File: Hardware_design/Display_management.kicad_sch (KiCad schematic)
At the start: 0 parts

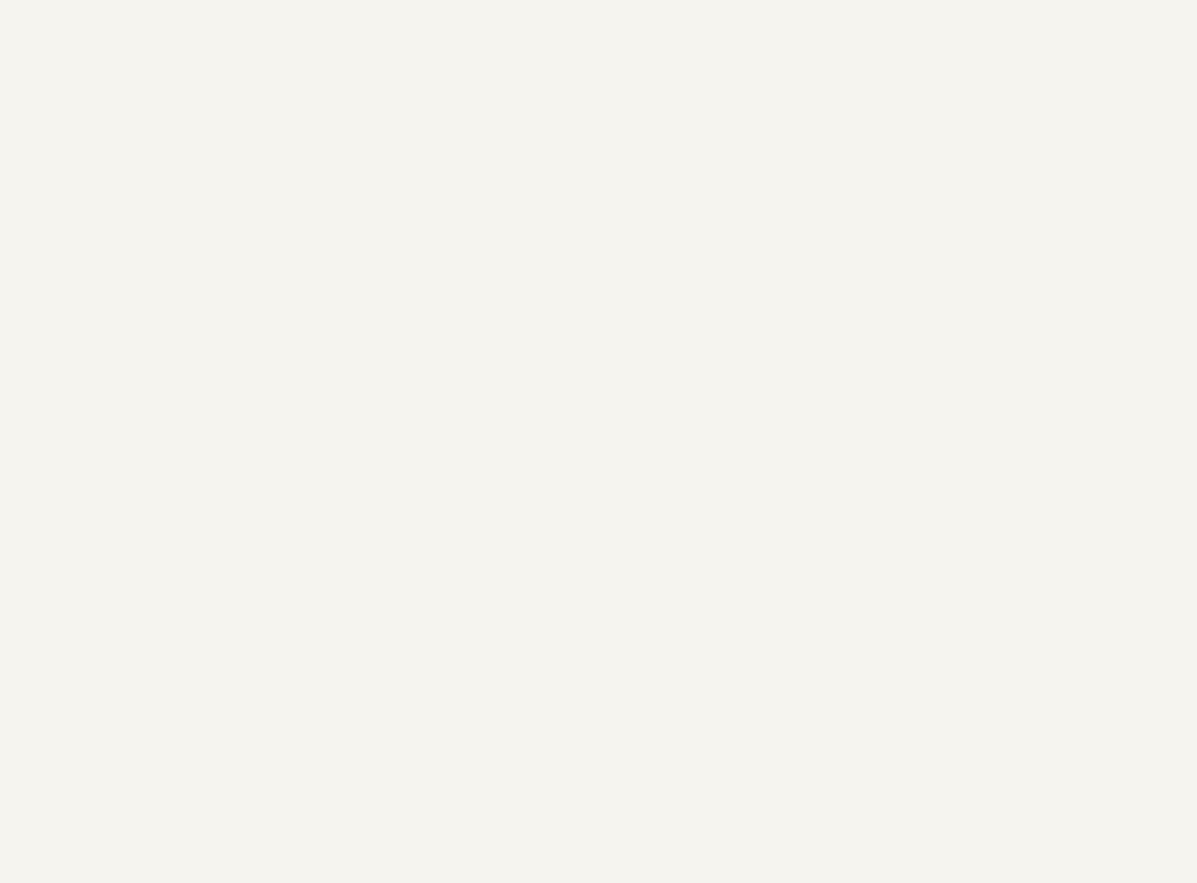
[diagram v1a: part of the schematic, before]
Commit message: STARTING THE DISPLAY design
acording to calculations we will need around 1.848 A when working with all the displays at the same time, including the MAX7221, the 1.848 A consumption is only for the display part.
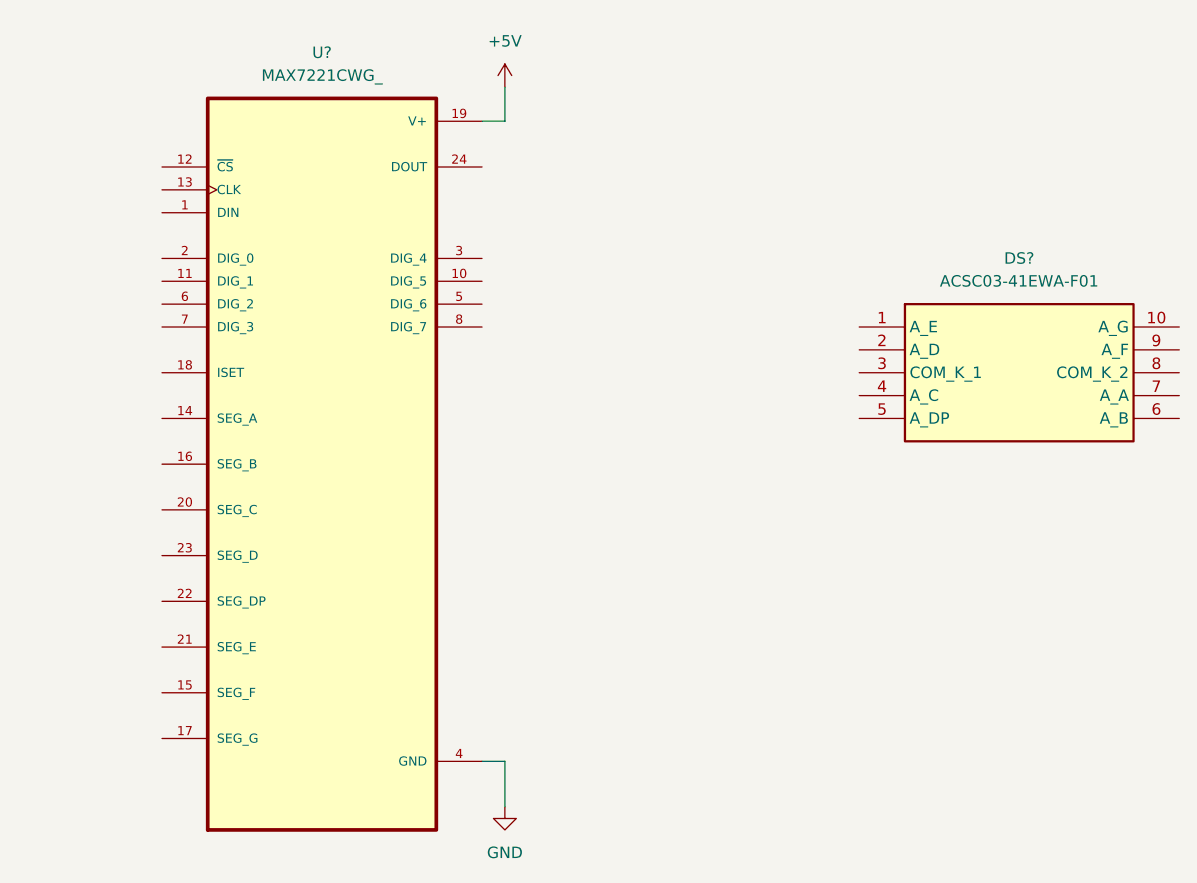
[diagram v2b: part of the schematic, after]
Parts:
- added DS?: ACSC03-41EWA-F01, ACSC0341EWAF01, symbol SMD_DISPLAY_ACSC03-41EWA-F01:ACSC03-41EWA-F01
- added U?: MAX7221CWG_, MAX7221CWG_:SOIC127P1032X265-24N, symbol Disp_Controler_MAX7221CWG_:MAX7221CWG_
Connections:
- new net +5V: U?.19 (V+)
- new net GND: U?.4 (GND), U?.9 (GND)

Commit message: display set up completed
for the displays we will not need an aditional voltage regulator becuase we will use the direct conection from the 5V power supply of the circuit, it needs to be able to provide at least 3A, recomended will be 4A for all the displays and pcb chips to work properly
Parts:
- added C? (x11): 0.1 uF, symbol Device:C
- added DS? (x84): ACSC03-41EWA-F01, ACSC0341EWAF01, symbol SMD_DISPLAY_ACSC03-41EWA-F01:ACSC03-41EWA-F01
- added R? (x11): 3v=24.5k, 1.8v=29.8k, symbol Device:R
- added U? (x10): MAX7221CWG_, MAX7221CWG_:SOIC127P1032X265-24N, symbol Disp_Controler_MAX7221CWG_:MAX7221CWG_
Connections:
- net +5V: now also C?.1, C?.1, C?.1, C?.1, C?.1, C?.1, C?.1, C?.1, C?.1, C?.1, C?.1, R?.1, R?.1, R?.1, R?.1, R?.1, R?.1, R?.1, R?.1, R?.1, R?.1, R?.1, U?.19 (V+), U?.19 (V+), U?.19 (V+), U?.19 (V+), U?.19 (V+), U?.19 (V+), U?.19 (V+), U?.19 (V+), U?.19 (V+), U?.19 (V+)
- net CS_MAX7221: now also U?.12 (~{CS}), U?.12 (~{CS}), U?.12 (~{CS}), U?.12 (~{CS}), U?.12 (~{CS}), U?.12 (~{CS}), U?.12 (~{CS}), U?.12 (~{CS}), U?.12 (~{CS}), U?.12 (~{CS}), U?.12 (~{CS})
- net GND: now also C?.2, C?.2, C?.2, C?.2, C?.2, C?.2, C?.2, C?.2, C?.2, C?.2, C?.2, U?.4 (GND), U?.4 (GND), U?.4 (GND), U?.4 (GND), U?.4 (GND), U?.4 (GND), U?.4 (GND), U?.4 (GND), U?.4 (GND), U?.4 (GND), U?.9 (GND), U?.9 (GND), U?.9 (GND), U?.9 (GND), U?.9 (GND), U?.9 (GND), U?.9 (GND), U?.9 (GND), U?.9 (GND), U?.9 (GND)
- net MOSI_MAX7221: now also U?.1 (DIN)
- net SCK_MAX7221: now also U?.13 (CLK), U?.13 (CLK), U?.13 (CLK), U?.13 (CLK), U?.13 (CLK), U?.13 (CLK), U?.13 (CLK), U?.13 (CLK), U?.13 (CLK), U?.13 (CLK), U?.13 (CLK)
- net DIG_5_MAX7221_1: now reaches U?.10 (DIG_5)
- net DIG_5_MAX7221_1: now also DS?.3 (COM_K_1), DS?.8 (COM_K_2)
- net DIG_1_MAX7221_1: now reaches U?.11 (DIG_1)
- net DIG_1_MAX7221_1: now also DS?.3 (COM_K_1), DS?.8 (COM_K_2)
- net SEG_A_MAX7221_1: now reaches U?.14 (SEG_A)
- net SEG_A_MAX7221_1: now also DS?.7 (A_A), DS?.7 (A_A), DS?.7 (A_A), DS?.7 (A_A), DS?.7 (A_A), DS?.7 (A_A), DS?.7 (A_A), DS?.7 (A_A)
- net SEG_F_MAX7221_1: now reaches U?.15 (SEG_F)
- net SEG_F_MAX7221_1: now also DS?.9 (A_F), DS?.9 (A_F), DS?.9 (A_F), DS?.9 (A_F), DS?.9 (A_F), DS?.9 (A_F), DS?.9 (A_F), DS?.9 (A_F)
- net SEG_B_MAX7221_1: now reaches U?.16 (SEG_B)
- net SEG_B_MAX7221_1: now also DS?.6 (A_B), DS?.6 (A_B), DS?.6 (A_B), DS?.6 (A_B), DS?.6 (A_B), DS?.6 (A_B), DS?.6 (A_B), DS?.6 (A_B)
- net SEG_G_MAX7221_1: now reaches U?.17 (SEG_G)
- net SEG_G_MAX7221_1: now also DS?.10 (A_G), DS?.10 (A_G), DS?.10 (A_G), DS?.10 (A_G), DS?.10 (A_G), DS?.10 (A_G), DS?.10 (A_G), DS?.10 (A_G)
- net at U?.18 (ISET): now also R?.2
- net DIG_0_MAX7221_1: now reaches U?.2 (DIG_0)
- net DIG_0_MAX7221_1: now also DS?.3 (COM_K_1), DS?.8 (COM_K_2)
- net SEG_C_MAX7221_1: now reaches U?.20 (SEG_C)
- net SEG_C_MAX7221_1: now also DS?.4 (A_C), DS?.4 (A_C), DS?.4 (A_C), DS?.4 (A_C), DS?.4 (A_C), DS?.4 (A_C), DS?.4 (A_C), DS?.4 (A_C)
- net SEG_E_MAX7221_1: now reaches U?.21 (SEG_E)
- net SEG_E_MAX7221_1: now also DS?.1 (A_E), DS?.1 (A_E), DS?.1 (A_E), DS?.1 (A_E), DS?.1 (A_E), DS?.1 (A_E), DS?.1 (A_E), DS?.1 (A_E)
- net SEG_DP_MAX7221_1: now reaches U?.22 (SEG_DP)
- net SEG_DP_MAX7221_1: now also DS?.5 (A_DP), DS?.5 (A_DP), DS?.5 (A_DP), DS?.5 (A_DP), DS?.5 (A_DP), DS?.5 (A_DP), DS?.5 (A_DP), DS?.5 (A_DP)
- net SEG_D_MAX7221_1: now reaches U?.23 (SEG_D)
- net SEG_D_MAX7221_1: now also DS?.2 (A_D), DS?.2 (A_D), DS?.2 (A_D), DS?.2 (A_D), DS?.2 (A_D), DS?.2 (A_D), DS?.2 (A_D), DS?.2 (A_D)
- net at U?.24 (DOUT): now also U?.1 (DIN)
- net DIG_4_MAX7221_1: now reaches U?.3 (DIG_4)
- net DIG_4_MAX7221_1: now also DS?.3 (COM_K_1), DS?.8 (COM_K_2)
- net DIG_6_MAX7221_1: now reaches U?.5 (DIG_6)
- net DIG_6_MAX7221_1: now also DS?.3 (COM_K_1), DS?.8 (COM_K_2)
- net DIG_2_MAX7221_1: now reaches U?.6 (DIG_2)
- net DIG_2_MAX7221_1: now also DS?.3 (COM_K_1), DS?.8 (COM_K_2)
- net DIG_3_MAX7221_1: now reaches U?.7 (DIG_3)
- net DIG_3_MAX7221_1: now also DS?.3 (COM_K_1), DS?.8 (COM_K_2)
- net DIG_7_MAX7221_1: now reaches U?.8 (DIG_7)
- net DIG_7_MAX7221_1: now also DS?.3 (COM_K_1), DS?.8 (COM_K_2)
- new net: R?.2, U?.18 (ISET) (x10)
- new net: U?.1 (DIN), U?.24 (DOUT) (x9)
- new net DIG_0_MAX7221_10: DS?.3 (COM_K_1), DS?.8 (COM_K_2), U?.2 (DIG_0)
- new net DIG_0_MAX7221_11: DS?.3 (COM_K_1), DS?.8 (COM_K_2), U?.2 (DIG_0)
- new net DIG_0_MAX7221_2: DS?.3 (COM_K_1), DS?.8 (COM_K_2), U?.2 (DIG_0)
- new net DIG_0_MAX7221_3: DS?.3 (COM_K_1), DS?.8 (COM_K_2), U?.2 (DIG_0)
- new net DIG_0_MAX7221_4: DS?.3 (COM_K_1), DS?.8 (COM_K_2), U?.2 (DIG_0)
- new net DIG_0_MAX7221_5: DS?.3 (COM_K_1), DS?.8 (COM_K_2), U?.2 (DIG_0)
- new net DIG_0_MAX7221_6: DS?.3 (COM_K_1), DS?.8 (COM_K_2), U?.2 (DIG_0)
- new net DIG_0_MAX7221_7: DS?.3 (COM_K_1), DS?.8 (COM_K_2), U?.2 (DIG_0)
- new net DIG_0_MAX7221_8: DS?.3 (COM_K_1), DS?.8 (COM_K_2), U?.2 (DIG_0)
- new net DIG_0_MAX7221_9: DS?.3 (COM_K_1), DS?.8 (COM_K_2), U?.2 (DIG_0)
- new net DIG_1_MAX7221_10: DS?.3 (COM_K_1), DS?.8 (COM_K_2), U?.11 (DIG_1)
- new net DIG_1_MAX7221_11: DS?.3 (COM_K_1), DS?.8 (COM_K_2), U?.11 (DIG_1)
- new net DIG_1_MAX7221_2: DS?.3 (COM_K_1), DS?.8 (COM_K_2), U?.11 (DIG_1)
- new net DIG_1_MAX7221_3: DS?.3 (COM_K_1), DS?.8 (COM_K_2), U?.11 (DIG_1)
- new net DIG_1_MAX7221_4: DS?.3 (COM_K_1), DS?.8 (COM_K_2), U?.11 (DIG_1)
- new net DIG_1_MAX7221_5: DS?.3 (COM_K_1), DS?.8 (COM_K_2), U?.11 (DIG_1)
- new net DIG_1_MAX7221_6: DS?.3 (COM_K_1), DS?.8 (COM_K_2), U?.11 (DIG_1)
- new net DIG_1_MAX7221_7: DS?.3 (COM_K_1), DS?.8 (COM_K_2), U?.11 (DIG_1)
- new net DIG_1_MAX7221_8: DS?.3 (COM_K_1), DS?.8 (COM_K_2), U?.11 (DIG_1)
- new net DIG_1_MAX7221_9: DS?.3 (COM_K_1), DS?.8 (COM_K_2), U?.11 (DIG_1)
- new net DIG_2_MAX7221_10: DS?.3 (COM_K_1), DS?.8 (COM_K_2), U?.6 (DIG_2)
- new net DIG_2_MAX7221_11: DS?.3 (COM_K_1), DS?.8 (COM_K_2), U?.6 (DIG_2)
- new net DIG_2_MAX7221_2: DS?.3 (COM_K_1), DS?.8 (COM_K_2), U?.6 (DIG_2)
- new net DIG_2_MAX7221_3: DS?.3 (COM_K_1), DS?.8 (COM_K_2), U?.6 (DIG_2)
- new net DIG_2_MAX7221_4: DS?.3 (COM_K_1), DS?.8 (COM_K_2), U?.6 (DIG_2)
- new net DIG_2_MAX7221_5: DS?.3 (COM_K_1), DS?.8 (COM_K_2), U?.6 (DIG_2)
- new net DIG_2_MAX7221_6: DS?.3 (COM_K_1), DS?.8 (COM_K_2), U?.6 (DIG_2)
- new net DIG_2_MAX7221_7: DS?.3 (COM_K_1), DS?.8 (COM_K_2), U?.6 (DIG_2)
- new net DIG_2_MAX7221_8: DS?.3 (COM_K_1), DS?.8 (COM_K_2), U?.6 (DIG_2)
- new net DIG_2_MAX7221_9: DS?.3 (COM_K_1), DS?.8 (COM_K_2), U?.6 (DIG_2)
- new net DIG_3_MAX7221_10: DS?.3 (COM_K_1), DS?.8 (COM_K_2), U?.7 (DIG_3)
- new net DIG_3_MAX7221_11: DS?.3 (COM_K_1), DS?.8 (COM_K_2), U?.7 (DIG_3)
- new net DIG_3_MAX7221_2: DS?.3 (COM_K_1), DS?.8 (COM_K_2), U?.7 (DIG_3)
- new net DIG_3_MAX7221_3: DS?.3 (COM_K_1), DS?.8 (COM_K_2), U?.7 (DIG_3)
- new net DIG_3_MAX7221_4: DS?.3 (COM_K_1), DS?.8 (COM_K_2), U?.7 (DIG_3)
- new net DIG_3_MAX7221_5: DS?.3 (COM_K_1), DS?.8 (COM_K_2), U?.7 (DIG_3)
- new net DIG_3_MAX7221_6: DS?.3 (COM_K_1), DS?.8 (COM_K_2), U?.7 (DIG_3)
- new net DIG_3_MAX7221_7: DS?.3 (COM_K_1), DS?.8 (COM_K_2), U?.7 (DIG_3)
- new net DIG_3_MAX7221_8: DS?.3 (COM_K_1), DS?.8 (COM_K_2), U?.7 (DIG_3)
- new net DIG_3_MAX7221_9: DS?.3 (COM_K_1), DS?.8 (COM_K_2), U?.7 (DIG_3)
- new net DIG_4_MAX7221_10: DS?.3 (COM_K_1), DS?.8 (COM_K_2), U?.3 (DIG_4)
- new net DIG_4_MAX7221_11: DS?.3 (COM_K_1), DS?.8 (COM_K_2), U?.3 (DIG_4)
- new net DIG_4_MAX7221_2: DS?.3 (COM_K_1), DS?.8 (COM_K_2), U?.3 (DIG_4)
- new net DIG_4_MAX7221_3: DS?.3 (COM_K_1), DS?.8 (COM_K_2), U?.3 (DIG_4)
- new net DIG_4_MAX7221_4: DS?.3 (COM_K_1), DS?.8 (COM_K_2), U?.3 (DIG_4)
- new net DIG_4_MAX7221_5: DS?.3 (COM_K_1), DS?.8 (COM_K_2), U?.3 (DIG_4)
- new net DIG_4_MAX7221_6: DS?.3 (COM_K_1), DS?.8 (COM_K_2), U?.3 (DIG_4)
- new net DIG_4_MAX7221_7: DS?.3 (COM_K_1), DS?.8 (COM_K_2), U?.3 (DIG_4)
- new net DIG_4_MAX7221_8: DS?.3 (COM_K_1), DS?.8 (COM_K_2), U?.3 (DIG_4)
- new net DIG_4_MAX7221_9: DS?.3 (COM_K_1), DS?.8 (COM_K_2), U?.3 (DIG_4)
- new net DIG_5_MAX7221_10: DS?.3 (COM_K_1), DS?.8 (COM_K_2), U?.10 (DIG_5)
- new net DIG_5_MAX7221_11: U?.10 (DIG_5)
- new net DIG_5_MAX7221_2: DS?.3 (COM_K_1), DS?.8 (COM_K_2), U?.10 (DIG_5)
- new net DIG_5_MAX7221_3: DS?.3 (COM_K_1), DS?.8 (COM_K_2), U?.10 (DIG_5)
- new net DIG_5_MAX7221_4: DS?.3 (COM_K_1), DS?.8 (COM_K_2), U?.10 (DIG_5)
- new net DIG_5_MAX7221_5: DS?.3 (COM_K_1), DS?.8 (COM_K_2), U?.10 (DIG_5)
- new net DIG_5_MAX7221_6: DS?.3 (COM_K_1), DS?.8 (COM_K_2), U?.10 (DIG_5)
- new net DIG_5_MAX7221_7: DS?.3 (COM_K_1), DS?.8 (COM_K_2), U?.10 (DIG_5)
- new net DIG_5_MAX7221_8: DS?.3 (COM_K_1), DS?.8 (COM_K_2), U?.10 (DIG_5)
- new net DIG_5_MAX7221_9: DS?.3 (COM_K_1), DS?.8 (COM_K_2), U?.10 (DIG_5)
- new net DIG_6_MAX7221_10: DS?.3 (COM_K_1), DS?.8 (COM_K_2), U?.5 (DIG_6)
- new net DIG_6_MAX7221_11: U?.5 (DIG_6)
- new net DIG_6_MAX7221_2: DS?.3 (COM_K_1), DS?.8 (COM_K_2), U?.5 (DIG_6)
- new net DIG_6_MAX7221_3: DS?.3 (COM_K_1), DS?.8 (COM_K_2), U?.5 (DIG_6)
- new net DIG_6_MAX7221_4: DS?.3 (COM_K_1), DS?.8 (COM_K_2), U?.5 (DIG_6)
- new net DIG_6_MAX7221_5: DS?.3 (COM_K_1), DS?.8 (COM_K_2), U?.5 (DIG_6)
- new net DIG_6_MAX7221_6: DS?.3 (COM_K_1), DS?.8 (COM_K_2), U?.5 (DIG_6)
- new net DIG_6_MAX7221_7: DS?.3 (COM_K_1), DS?.8 (COM_K_2), U?.5 (DIG_6)
- new net DIG_6_MAX7221_8: DS?.3 (COM_K_1), DS?.8 (COM_K_2), U?.5 (DIG_6)
- new net DIG_6_MAX7221_9: DS?.3 (COM_K_1), DS?.8 (COM_K_2), U?.5 (DIG_6)
- new net DIG_7_MAX7221_10: DS?.3 (COM_K_1), DS?.8 (COM_K_2), U?.8 (DIG_7)
- new net DIG_7_MAX7221_11: U?.8 (DIG_7)
- new net DIG_7_MAX7221_2: DS?.3 (COM_K_1), DS?.8 (COM_K_2), U?.8 (DIG_7)
- new net DIG_7_MAX7221_3: DS?.3 (COM_K_1), DS?.8 (COM_K_2), U?.8 (DIG_7)
- new net DIG_7_MAX7221_4: DS?.3 (COM_K_1), DS?.8 (COM_K_2), U?.8 (DIG_7)
- new net DIG_7_MAX7221_5: DS?.3 (COM_K_1), DS?.8 (COM_K_2), U?.8 (DIG_7)
- new net DIG_7_MAX7221_6: DS?.3 (COM_K_1), DS?.8 (COM_K_2), U?.8 (DIG_7)
- new net DIG_7_MAX7221_7: DS?.3 (COM_K_1), DS?.8 (COM_K_2), U?.8 (DIG_7)
- new net DIG_7_MAX7221_8: DS?.3 (COM_K_1), DS?.8 (COM_K_2), U?.8 (DIG_7)
- new net DIG_7_MAX7221_9: DS?.3 (COM_K_1), DS?.8 (COM_K_2), U?.8 (DIG_7)
- new net SEG_A_MAX7221_10: DS?.7 (A_A), DS?.7 (A_A), DS?.7 (A_A), DS?.7 (A_A), DS?.7 (A_A), DS?.7 (A_A), DS?.7 (A_A), DS?.7 (A_A), U?.14 (SEG_A)
- new net SEG_A_MAX7221_11: DS?.7 (A_A), DS?.7 (A_A), DS?.7 (A_A), DS?.7 (A_A), DS?.7 (A_A), U?.14 (SEG_A)
- new net SEG_A_MAX7221_2: DS?.7 (A_A), DS?.7 (A_A), DS?.7 (A_A), DS?.7 (A_A), DS?.7 (A_A), DS?.7 (A_A), DS?.7 (A_A), DS?.7 (A_A), U?.14 (SEG_A)
- new net SEG_A_MAX7221_3: DS?.7 (A_A), DS?.7 (A_A), DS?.7 (A_A), DS?.7 (A_A), DS?.7 (A_A), DS?.7 (A_A), DS?.7 (A_A), DS?.7 (A_A), U?.14 (SEG_A)
- new net SEG_A_MAX7221_4: DS?.7 (A_A), DS?.7 (A_A), DS?.7 (A_A), DS?.7 (A_A), DS?.7 (A_A), DS?.7 (A_A), DS?.7 (A_A), DS?.7 (A_A), U?.14 (SEG_A)
- new net SEG_A_MAX7221_5: DS?.7 (A_A), DS?.7 (A_A), DS?.7 (A_A), DS?.7 (A_A), DS?.7 (A_A), DS?.7 (A_A), DS?.7 (A_A), DS?.7 (A_A), U?.14 (SEG_A)
- new net SEG_A_MAX7221_6: DS?.7 (A_A), DS?.7 (A_A), DS?.7 (A_A), DS?.7 (A_A), DS?.7 (A_A), DS?.7 (A_A), DS?.7 (A_A), DS?.7 (A_A), U?.14 (SEG_A)
- new net SEG_A_MAX7221_7: DS?.7 (A_A), DS?.7 (A_A), DS?.7 (A_A), DS?.7 (A_A), DS?.7 (A_A), DS?.7 (A_A), DS?.7 (A_A), DS?.7 (A_A), U?.14 (SEG_A)
- new net SEG_A_MAX7221_8: DS?.7 (A_A), DS?.7 (A_A), DS?.7 (A_A), DS?.7 (A_A), DS?.7 (A_A), DS?.7 (A_A), DS?.7 (A_A), DS?.7 (A_A), U?.14 (SEG_A)
- new net SEG_A_MAX7221_9: DS?.7 (A_A), DS?.7 (A_A), DS?.7 (A_A), DS?.7 (A_A), DS?.7 (A_A), DS?.7 (A_A), DS?.7 (A_A), DS?.7 (A_A), U?.14 (SEG_A)
- new net SEG_B_MAX7221_10: DS?.6 (A_B), DS?.6 (A_B), DS?.6 (A_B), DS?.6 (A_B), DS?.6 (A_B), DS?.6 (A_B), DS?.6 (A_B), DS?.6 (A_B), U?.16 (SEG_B)
- new net SEG_B_MAX7221_11: DS?.6 (A_B), DS?.6 (A_B), DS?.6 (A_B), DS?.6 (A_B), DS?.6 (A_B), U?.16 (SEG_B)
- new net SEG_B_MAX7221_2: DS?.6 (A_B), DS?.6 (A_B), DS?.6 (A_B), DS?.6 (A_B), DS?.6 (A_B), DS?.6 (A_B), DS?.6 (A_B), DS?.6 (A_B), U?.16 (SEG_B)
- new net SEG_B_MAX7221_3: DS?.6 (A_B), DS?.6 (A_B), DS?.6 (A_B), DS?.6 (A_B), DS?.6 (A_B), DS?.6 (A_B), DS?.6 (A_B), DS?.6 (A_B), U?.16 (SEG_B)
- new net SEG_B_MAX7221_4: DS?.6 (A_B), DS?.6 (A_B), DS?.6 (A_B), DS?.6 (A_B), DS?.6 (A_B), DS?.6 (A_B), DS?.6 (A_B), DS?.6 (A_B), U?.16 (SEG_B)
- new net SEG_B_MAX7221_5: DS?.6 (A_B), DS?.6 (A_B), DS?.6 (A_B), DS?.6 (A_B), DS?.6 (A_B), DS?.6 (A_B), DS?.6 (A_B), DS?.6 (A_B), U?.16 (SEG_B)
- new net SEG_B_MAX7221_6: DS?.6 (A_B), DS?.6 (A_B), DS?.6 (A_B), DS?.6 (A_B), DS?.6 (A_B), DS?.6 (A_B), DS?.6 (A_B), DS?.6 (A_B), U?.16 (SEG_B)
- new net SEG_B_MAX7221_7: DS?.6 (A_B), DS?.6 (A_B), DS?.6 (A_B), DS?.6 (A_B), DS?.6 (A_B), DS?.6 (A_B), DS?.6 (A_B), DS?.6 (A_B), U?.16 (SEG_B)
- new net SEG_B_MAX7221_8: DS?.6 (A_B), DS?.6 (A_B), DS?.6 (A_B), DS?.6 (A_B), DS?.6 (A_B), DS?.6 (A_B), DS?.6 (A_B), DS?.6 (A_B), U?.16 (SEG_B)
- new net SEG_B_MAX7221_9: DS?.6 (A_B), DS?.6 (A_B), DS?.6 (A_B), DS?.6 (A_B), DS?.6 (A_B), DS?.6 (A_B), DS?.6 (A_B), DS?.6 (A_B), U?.16 (SEG_B)
- new net SEG_C_MAX7221_10: DS?.4 (A_C), DS?.4 (A_C), DS?.4 (A_C), DS?.4 (A_C), DS?.4 (A_C), DS?.4 (A_C), DS?.4 (A_C), DS?.4 (A_C), U?.20 (SEG_C)
- new net SEG_C_MAX7221_11: DS?.4 (A_C), DS?.4 (A_C), DS?.4 (A_C), DS?.4 (A_C), DS?.4 (A_C), U?.20 (SEG_C)
- new net SEG_C_MAX7221_2: DS?.4 (A_C), DS?.4 (A_C), DS?.4 (A_C), DS?.4 (A_C), DS?.4 (A_C), DS?.4 (A_C), DS?.4 (A_C), DS?.4 (A_C), U?.20 (SEG_C)
- new net SEG_C_MAX7221_3: DS?.4 (A_C), DS?.4 (A_C), DS?.4 (A_C), DS?.4 (A_C), DS?.4 (A_C), DS?.4 (A_C), DS?.4 (A_C), DS?.4 (A_C), U?.20 (SEG_C)
- new net SEG_C_MAX7221_4: DS?.4 (A_C), DS?.4 (A_C), DS?.4 (A_C), DS?.4 (A_C), DS?.4 (A_C), DS?.4 (A_C), DS?.4 (A_C), DS?.4 (A_C), U?.20 (SEG_C)
- new net SEG_C_MAX7221_5: DS?.4 (A_C), DS?.4 (A_C), DS?.4 (A_C), DS?.4 (A_C), DS?.4 (A_C), DS?.4 (A_C), DS?.4 (A_C), DS?.4 (A_C), U?.20 (SEG_C)
- new net SEG_C_MAX7221_6: DS?.4 (A_C), DS?.4 (A_C), DS?.4 (A_C), DS?.4 (A_C), DS?.4 (A_C), DS?.4 (A_C), DS?.4 (A_C), DS?.4 (A_C), U?.20 (SEG_C)
- new net SEG_C_MAX7221_7: DS?.4 (A_C), DS?.4 (A_C), DS?.4 (A_C), DS?.4 (A_C), DS?.4 (A_C), DS?.4 (A_C), DS?.4 (A_C), DS?.4 (A_C), U?.20 (SEG_C)
- new net SEG_C_MAX7221_8: DS?.4 (A_C), DS?.4 (A_C), DS?.4 (A_C), DS?.4 (A_C), DS?.4 (A_C), DS?.4 (A_C), DS?.4 (A_C), DS?.4 (A_C), U?.20 (SEG_C)
- new net SEG_C_MAX7221_9: DS?.4 (A_C), DS?.4 (A_C), DS?.4 (A_C), DS?.4 (A_C), DS?.4 (A_C), DS?.4 (A_C), DS?.4 (A_C), DS?.4 (A_C), U?.20 (SEG_C)
- new net SEG_DP_MAX7221_10: DS?.5 (A_DP), DS?.5 (A_DP), DS?.5 (A_DP), DS?.5 (A_DP), DS?.5 (A_DP), DS?.5 (A_DP), DS?.5 (A_DP), DS?.5 (A_DP), U?.22 (SEG_DP)
- new net SEG_DP_MAX7221_11: DS?.5 (A_DP), DS?.5 (A_DP), DS?.5 (A_DP), DS?.5 (A_DP), DS?.5 (A_DP), U?.22 (SEG_DP)
- new net SEG_DP_MAX7221_2: DS?.5 (A_DP), DS?.5 (A_DP), DS?.5 (A_DP), DS?.5 (A_DP), DS?.5 (A_DP), DS?.5 (A_DP), DS?.5 (A_DP), DS?.5 (A_DP), U?.22 (SEG_DP)
- new net SEG_DP_MAX7221_3: DS?.5 (A_DP), DS?.5 (A_DP), DS?.5 (A_DP), DS?.5 (A_DP), DS?.5 (A_DP), DS?.5 (A_DP), DS?.5 (A_DP), DS?.5 (A_DP), U?.22 (SEG_DP)
- new net SEG_DP_MAX7221_4: DS?.5 (A_DP), DS?.5 (A_DP), DS?.5 (A_DP), DS?.5 (A_DP), DS?.5 (A_DP), DS?.5 (A_DP), DS?.5 (A_DP), DS?.5 (A_DP), U?.22 (SEG_DP)
- new net SEG_DP_MAX7221_5: DS?.5 (A_DP), DS?.5 (A_DP), DS?.5 (A_DP), DS?.5 (A_DP), DS?.5 (A_DP), DS?.5 (A_DP), DS?.5 (A_DP), DS?.5 (A_DP), U?.22 (SEG_DP)
- new net SEG_DP_MAX7221_6: DS?.5 (A_DP), DS?.5 (A_DP), DS?.5 (A_DP), DS?.5 (A_DP), DS?.5 (A_DP), DS?.5 (A_DP), DS?.5 (A_DP), DS?.5 (A_DP), U?.22 (SEG_DP)
- new net SEG_DP_MAX7221_7: DS?.5 (A_DP), DS?.5 (A_DP), DS?.5 (A_DP), DS?.5 (A_DP), DS?.5 (A_DP), DS?.5 (A_DP), DS?.5 (A_DP), DS?.5 (A_DP), U?.22 (SEG_DP)
- new net SEG_DP_MAX7221_8: DS?.5 (A_DP), DS?.5 (A_DP), DS?.5 (A_DP), DS?.5 (A_DP), DS?.5 (A_DP), DS?.5 (A_DP), DS?.5 (A_DP), DS?.5 (A_DP), U?.22 (SEG_DP)
- new net SEG_DP_MAX7221_9: DS?.5 (A_DP), DS?.5 (A_DP), DS?.5 (A_DP), DS?.5 (A_DP), DS?.5 (A_DP), DS?.5 (A_DP), DS?.5 (A_DP), DS?.5 (A_DP), U?.22 (SEG_DP)
- new net SEG_D_MAX7221_10: DS?.2 (A_D), DS?.2 (A_D), DS?.2 (A_D), DS?.2 (A_D), DS?.2 (A_D), DS?.2 (A_D), DS?.2 (A_D), DS?.2 (A_D), U?.23 (SEG_D)
- new net SEG_D_MAX7221_11: DS?.2 (A_D), DS?.2 (A_D), DS?.2 (A_D), DS?.2 (A_D), DS?.2 (A_D), U?.23 (SEG_D)
- new net SEG_D_MAX7221_2: DS?.2 (A_D), DS?.2 (A_D), DS?.2 (A_D), DS?.2 (A_D), DS?.2 (A_D), DS?.2 (A_D), DS?.2 (A_D), DS?.2 (A_D), U?.23 (SEG_D)
- new net SEG_D_MAX7221_3: DS?.2 (A_D), DS?.2 (A_D), DS?.2 (A_D), DS?.2 (A_D), DS?.2 (A_D), DS?.2 (A_D), DS?.2 (A_D), DS?.2 (A_D), U?.23 (SEG_D)
- new net SEG_D_MAX7221_4: DS?.2 (A_D), DS?.2 (A_D), DS?.2 (A_D), DS?.2 (A_D), DS?.2 (A_D), DS?.2 (A_D), DS?.2 (A_D), DS?.2 (A_D), U?.23 (SEG_D)
- new net SEG_D_MAX7221_5: DS?.2 (A_D), DS?.2 (A_D), DS?.2 (A_D), DS?.2 (A_D), DS?.2 (A_D), DS?.2 (A_D), DS?.2 (A_D), DS?.2 (A_D), U?.23 (SEG_D)
- new net SEG_D_MAX7221_6: DS?.2 (A_D), DS?.2 (A_D), DS?.2 (A_D), DS?.2 (A_D), DS?.2 (A_D), DS?.2 (A_D), DS?.2 (A_D), DS?.2 (A_D), U?.23 (SEG_D)
- new net SEG_D_MAX7221_7: DS?.2 (A_D), DS?.2 (A_D), DS?.2 (A_D), DS?.2 (A_D), DS?.2 (A_D), DS?.2 (A_D), DS?.2 (A_D), DS?.2 (A_D), U?.23 (SEG_D)
- new net SEG_D_MAX7221_8: DS?.2 (A_D), DS?.2 (A_D), DS?.2 (A_D), DS?.2 (A_D), DS?.2 (A_D), DS?.2 (A_D), DS?.2 (A_D), DS?.2 (A_D), U?.23 (SEG_D)
- new net SEG_D_MAX7221_9: DS?.2 (A_D), DS?.2 (A_D), DS?.2 (A_D), DS?.2 (A_D), DS?.2 (A_D), DS?.2 (A_D), DS?.2 (A_D), DS?.2 (A_D), U?.23 (SEG_D)
- new net SEG_E_MAX7221_10: DS?.1 (A_E), DS?.1 (A_E), DS?.1 (A_E), DS?.1 (A_E), DS?.1 (A_E), DS?.1 (A_E), DS?.1 (A_E), DS?.1 (A_E), U?.21 (SEG_E)
- new net SEG_E_MAX7221_11: DS?.1 (A_E), DS?.1 (A_E), DS?.1 (A_E), DS?.1 (A_E), DS?.1 (A_E), U?.21 (SEG_E)
- new net SEG_E_MAX7221_2: DS?.1 (A_E), DS?.1 (A_E), DS?.1 (A_E), DS?.1 (A_E), DS?.1 (A_E), DS?.1 (A_E), DS?.1 (A_E), DS?.1 (A_E), U?.21 (SEG_E)
- new net SEG_E_MAX7221_3: DS?.1 (A_E), DS?.1 (A_E), DS?.1 (A_E), DS?.1 (A_E), DS?.1 (A_E), DS?.1 (A_E), DS?.1 (A_E), DS?.1 (A_E), U?.21 (SEG_E)
- new net SEG_E_MAX7221_4: DS?.1 (A_E), DS?.1 (A_E), DS?.1 (A_E), DS?.1 (A_E), DS?.1 (A_E), DS?.1 (A_E), DS?.1 (A_E), DS?.1 (A_E), U?.21 (SEG_E)
- new net SEG_E_MAX7221_5: DS?.1 (A_E), DS?.1 (A_E), DS?.1 (A_E), DS?.1 (A_E), DS?.1 (A_E), DS?.1 (A_E), DS?.1 (A_E), DS?.1 (A_E), U?.21 (SEG_E)
- new net SEG_E_MAX7221_6: DS?.1 (A_E), DS?.1 (A_E), DS?.1 (A_E), DS?.1 (A_E), DS?.1 (A_E), DS?.1 (A_E), DS?.1 (A_E), DS?.1 (A_E), U?.21 (SEG_E)
- new net SEG_E_MAX7221_7: DS?.1 (A_E), DS?.1 (A_E), DS?.1 (A_E), DS?.1 (A_E), DS?.1 (A_E), DS?.1 (A_E), DS?.1 (A_E), DS?.1 (A_E), U?.21 (SEG_E)
- new net SEG_E_MAX7221_8: DS?.1 (A_E), DS?.1 (A_E), DS?.1 (A_E), DS?.1 (A_E), DS?.1 (A_E), DS?.1 (A_E), DS?.1 (A_E), DS?.1 (A_E), U?.21 (SEG_E)
- new net SEG_E_MAX7221_9: DS?.1 (A_E), DS?.1 (A_E), DS?.1 (A_E), DS?.1 (A_E), DS?.1 (A_E), DS?.1 (A_E), DS?.1 (A_E), DS?.1 (A_E), U?.21 (SEG_E)
- new net SEG_F_MAX7221_10: DS?.9 (A_F), DS?.9 (A_F), DS?.9 (A_F), DS?.9 (A_F), DS?.9 (A_F), DS?.9 (A_F), DS?.9 (A_F), DS?.9 (A_F), U?.15 (SEG_F)
- new net SEG_F_MAX7221_11: DS?.9 (A_F), DS?.9 (A_F), DS?.9 (A_F), DS?.9 (A_F), DS?.9 (A_F), U?.15 (SEG_F)
- new net SEG_F_MAX7221_2: DS?.9 (A_F), DS?.9 (A_F), DS?.9 (A_F), DS?.9 (A_F), DS?.9 (A_F), DS?.9 (A_F), DS?.9 (A_F), DS?.9 (A_F), U?.15 (SEG_F)
- new net SEG_F_MAX7221_3: DS?.9 (A_F), DS?.9 (A_F), DS?.9 (A_F), DS?.9 (A_F), DS?.9 (A_F), DS?.9 (A_F), DS?.9 (A_F), DS?.9 (A_F), U?.15 (SEG_F)
- new net SEG_F_MAX7221_4: DS?.9 (A_F), DS?.9 (A_F), DS?.9 (A_F), DS?.9 (A_F), DS?.9 (A_F), DS?.9 (A_F), DS?.9 (A_F), DS?.9 (A_F), U?.15 (SEG_F)
- new net SEG_F_MAX7221_5: DS?.9 (A_F), DS?.9 (A_F), DS?.9 (A_F), DS?.9 (A_F), DS?.9 (A_F), DS?.9 (A_F), DS?.9 (A_F), DS?.9 (A_F), U?.15 (SEG_F)
- new net SEG_F_MAX7221_6: DS?.9 (A_F), DS?.9 (A_F), DS?.9 (A_F), DS?.9 (A_F), DS?.9 (A_F), DS?.9 (A_F), DS?.9 (A_F), DS?.9 (A_F), U?.15 (SEG_F)
- new net SEG_F_MAX7221_7: DS?.9 (A_F), DS?.9 (A_F), DS?.9 (A_F), DS?.9 (A_F), DS?.9 (A_F), DS?.9 (A_F), DS?.9 (A_F), DS?.9 (A_F), U?.15 (SEG_F)
- new net SEG_F_MAX7221_8: DS?.9 (A_F), DS?.9 (A_F), DS?.9 (A_F), DS?.9 (A_F), DS?.9 (A_F), DS?.9 (A_F), DS?.9 (A_F), DS?.9 (A_F), U?.15 (SEG_F)
- new net SEG_F_MAX7221_9: DS?.9 (A_F), DS?.9 (A_F), DS?.9 (A_F), DS?.9 (A_F), DS?.9 (A_F), DS?.9 (A_F), DS?.9 (A_F), DS?.9 (A_F), U?.15 (SEG_F)
- new net SEG_G_MAX7221_10: DS?.10 (A_G), DS?.10 (A_G), DS?.10 (A_G), DS?.10 (A_G), DS?.10 (A_G), DS?.10 (A_G), DS?.10 (A_G), DS?.10 (A_G), U?.17 (SEG_G)
- new net SEG_G_MAX7221_11: DS?.10 (A_G), DS?.10 (A_G), DS?.10 (A_G), DS?.10 (A_G), DS?.10 (A_G), U?.17 (SEG_G)
- new net SEG_G_MAX7221_2: DS?.10 (A_G), DS?.10 (A_G), DS?.10 (A_G), DS?.10 (A_G), DS?.10 (A_G), DS?.10 (A_G), DS?.10 (A_G), DS?.10 (A_G), U?.17 (SEG_G)
- new net SEG_G_MAX7221_3: DS?.10 (A_G), DS?.10 (A_G), DS?.10 (A_G), DS?.10 (A_G), DS?.10 (A_G), DS?.10 (A_G), DS?.10 (A_G), DS?.10 (A_G), U?.17 (SEG_G)
- new net SEG_G_MAX7221_4: DS?.10 (A_G), DS?.10 (A_G), DS?.10 (A_G), DS?.10 (A_G), DS?.10 (A_G), DS?.10 (A_G), DS?.10 (A_G), DS?.10 (A_G), U?.17 (SEG_G)
- new net SEG_G_MAX7221_5: DS?.10 (A_G), DS?.10 (A_G), DS?.10 (A_G), DS?.10 (A_G), DS?.10 (A_G), DS?.10 (A_G), DS?.10 (A_G), DS?.10 (A_G), U?.17 (SEG_G)
- new net SEG_G_MAX7221_6: DS?.10 (A_G), DS?.10 (A_G), DS?.10 (A_G), DS?.10 (A_G), DS?.10 (A_G), DS?.10 (A_G), DS?.10 (A_G), DS?.10 (A_G), U?.17 (SEG_G)
- new net SEG_G_MAX7221_7: DS?.10 (A_G), DS?.10 (A_G), DS?.10 (A_G), DS?.10 (A_G), DS?.10 (A_G), DS?.10 (A_G), DS?.10 (A_G), DS?.10 (A_G), U?.17 (SEG_G)
- new net SEG_G_MAX7221_8: DS?.10 (A_G), DS?.10 (A_G), DS?.10 (A_G), DS?.10 (A_G), DS?.10 (A_G), DS?.10 (A_G), DS?.10 (A_G), DS?.10 (A_G), U?.17 (SEG_G)
- new net SEG_G_MAX7221_9: DS?.10 (A_G), DS?.10 (A_G), DS?.10 (A_G), DS?.10 (A_G), DS?.10 (A_G), DS?.10 (A_G), DS?.10 (A_G), DS?.10 (A_G), U?.17 (SEG_G)
- no-connect marks 0 -> 1
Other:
- note added: "1"
- note added: "10"
- note added: "11"
- note added: "2"
- note added: "3"
- note added: "4"
- note added: "5"
- note added: "6"
- note added: "7"
- note added: "8"
- note added: "9"
- moved on the sheet: DS?

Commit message: starting footprint asignment
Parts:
- added C38, C39, C40, C41, C42, C43, C44, C45, C46, C47, C48: 10uF, Footprints:0805_SMD_TANT_CAP_T491B106K016AT, symbol Device:C
- added TP10, TP11, TP12, TP13, TP14, TP15, TP16, TP17, TP8, TP9: TestPoint, symbol Connector:TestPoint
- C14, C15, C16, C17, C18, C19, C20, C21, C22, C23, C24: renamed from C?; footprint (none) -> Footprints:0805_SMD_CERAMIC_CAP_T491B106K016AT
- DS1, DS10, DS11, DS12, DS13, DS14, DS15, DS16, DS17, DS18, DS19, DS2, DS20, DS21, DS22, DS23, DS24, DS25, DS26, DS27, DS28, DS29, DS3, DS30, DS31, DS32, DS33, DS34, DS35, DS36, DS37, DS38, DS39, DS4, DS40, DS41, DS42, DS43, DS44, DS45, DS46, DS47, DS48, DS49, DS5, DS50, DS51, DS52, DS53, DS54, DS55, DS56, DS57, DS58, DS59, DS6, DS60, DS61, DS62, DS63, DS64, DS65, DS66, DS67, DS68, DS69, DS7, DS70, DS71, DS72, DS73, DS74, DS75, DS76, DS77, DS78, DS79, DS8, DS80, DS81, DS82, DS83, DS84, DS85, DS9: renamed from DS?; footprint ACSC0341EWAF01 -> Footprints:SMD_DISPLAY_ACSC03-41EWA-F01
- U10, U11, U12, U13, U14, U4, U5, U6, U7, U8, U9: renamed from U?; footprint MAX7221CWG_:SOIC127P1032X265-24N -> Footprints:Disp_Controler_MAX7221CWG_
- gave numbers to parts that had none: 11
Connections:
- net +5V: now also C38.1, C39.1, C40.1, C41.1, C42.1, C43.1, C44.1, C45.1, C46.1, C47.1, C48.1
- net GND: now also C38.2, C39.2, C40.2, C41.2, C42.2, C43.2, C44.2, C45.2, C46.2, C47.2, C48.2
- net at U4.24 (DOUT), U5.1 (DIN): now also TP8.1
- net at U5.24 (DOUT), U6.1 (DIN): now also TP9.1
- net at U6.24 (DOUT), U7.1 (DIN): now also TP10.1
- net at U13.24 (DOUT), U14.1 (DIN): now also TP17.1
- net at U8.24 (DOUT), U9.1 (DIN): now also TP12.1
- net at U10.1 (DIN), U9.24 (DOUT): now also TP13.1
- net at U10.24 (DOUT), U11.1 (DIN): now also TP14.1
- net at U11.24 (DOUT), U12.1 (DIN): now also TP15.1
- net at U7.24 (DOUT), U8.1 (DIN): now also TP11.1
- net at U12.24 (DOUT), U13.1 (DIN): now also TP16.1
- net CS_MAX7221 renamed CS_MAX7221_5V
- net MOSI_MAX7221 renamed MOSI_MAX7221_5V
- net SCK_MAX7221 renamed SCK_MAX7221_5V
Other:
- moved on the sheet: C20

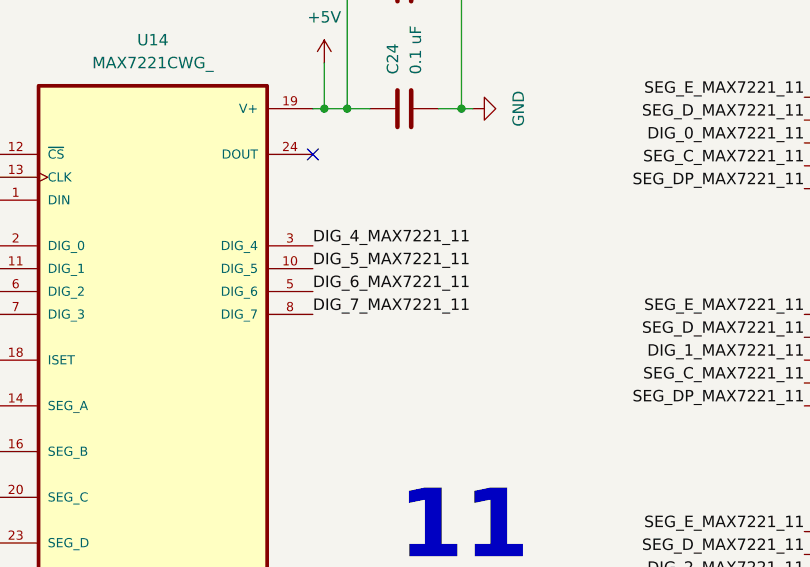
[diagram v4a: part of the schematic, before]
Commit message: all footprints asigned
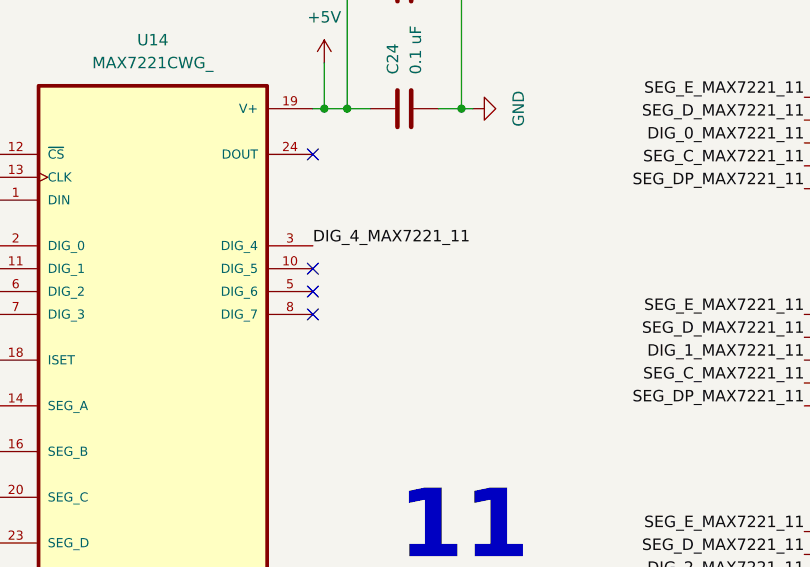
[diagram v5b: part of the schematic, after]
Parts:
- R12, R13, R14, R15, R16, R17, R18, R19, R20, R21, R22: footprint (none) -> Footprints:0805_RES_RESC2012X60N
- TP10, TP11, TP12, TP13, TP14, TP15, TP16, TP17, TP8, TP9: footprint (none) -> TestPoint:TestPoint_Pad_1.0x1.0mm
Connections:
- net DIG_5_MAX7221_11: no longer names the net of U14.10 (DIG_5)
- net DIG_6_MAX7221_11: no longer names the net of U14.5 (DIG_6)
- net DIG_7_MAX7221_11: no longer names the net of U14.8 (DIG_7)
- no-connect marks 1 -> 4
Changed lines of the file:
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@@
 	)
 	(no_connect
+		(at 109.22 1228.09)
+	)
+	(no_connect
 		(at 109.22 1215.39)
 	)
+	(no_connect
+		(at 109.22 1233.17)
+	)
+	(no_connect
+		(at 109.22 1230.63)
+	)
 	(wire
 		(pts
@@
 		)
 	)
-	(label "DIG_7_MAX7221_11"
-		(at 109.22 1233.17 0)
-		(effects
-			(font
-				(size 1.27 1.27)
-			)
-			(justify left bottom)
-		)
-	)
 	(label "SEG_D_MAX7221_3"
 		(at 242.57 302.26 180)
@@
 		)
 	)
-	(label "DIG_6_MAX7221_11"
-		(at 109.22 1230.63 0)
-		(effects
-			(font
-				(size 1.27 1.27)
-			)
-			(justify left bottom)
-		)
-	)
 	(label "DIG_0_MAX7221_8"
 		(at 199.39 867.41 0)
@@
 		)
 	)
-	(label "DIG_5_MAX7221_11"
-		(at 109.22 1228.09 0)
-		(effects
-			(font
-				(size 1.27 1.27)
-			)
-			(justify left bottom)
-		)
-	)
 	(label "DIG_4_MAX7221_11"
 		(at 242.57 1214.12 180)
@@
 			)
 		)
-		(property "Footprint" ""
+		(property "Footprint" "TestPoint:TestPoint_Pad_1.0x1.0mm"
 			(at 139.7 998.22 0)
 			(hide yes)
@@
 			)
 		)
-		(property "Footprint" ""
+		(property "Footprint" "Footprints:0805_RES_RESC2012X60N"
 			(at 49.022 529.59 90)
 			(hide yes)
@@
 			)
 		)
-		(property "Footprint" ""
+		(property "Footprint" "Footprints:0805_RES_RESC2012X60N"
 			(at 49.022 764.54 90)
 			(hide yes)
@@
 			)
 		)
-		(property "Footprint" ""
+		(property "Footprint" "Footprints:0805_RES_RESC2012X60N"
 			(at 49.022 68.58 90)
 			(hide yes)
@@
 			)
 		)
-		(property "Footprint" ""
+		(property "Footprint" "TestPoint:TestPoint_Pad_1.0x1.0mm"
 			(at 135.89 185.42 0)
 			(hide yes)
@@
 			)
 		)
-		(property "Footprint" ""
+		(property "Footprint" "TestPoint:TestPoint_Pad_1.0x1.0mm"
 			(at 135.89 71.12 0)
 			(hide yes)
@@
 			)
 		)
-		(property "Footprint" ""
+		(property "Footprint" "Footprints:0805_RES_RESC2012X60N"
 			(at 49.022 1228.09 90)
 			(hide yes)
@@
 			)
 		)
-		(property "Footprint" ""
+		(property "Footprint" "TestPoint:TestPoint_Pad_1.0x1.0mm"
 			(at 139.7 885.19 0)
 			(hide yes)
@@
 			)
 		)
-		(property "Footprint" ""
+		(property "Footprint" "TestPoint:TestPoint_Pad_1.0x1.0mm"
 			(at 140.97 420.37 0)
 			(hide yes)
@@
 			)
 		)
-		(property "Footprint" ""
+		(property "Footprint" "Footprints:0805_RES_RESC2012X60N"
 			(at 49.022 995.68 90)
 			(hide yes)
@@
 			)
 		)
-		(property "Footprint" ""
+		(property "Footprint" "TestPoint:TestPoint_Pad_1.0x1.0mm"
 			(at 139.7 654.05 0)
 			(hide yes)
@@
 			)
 		)
-		(property "Footprint" ""
+		(property "Footprint" "TestPoint:TestPoint_Pad_1.0x1.0mm"
 			(at 139.7 1113.79 0)
 			(hide yes)
@@
 			)
 		)
-		(property "Footprint" ""
+		(property "Footprint" "Footprints:0805_RES_RESC2012X60N"
 			(at 49.022 415.29 90)
 			(hide yes)
@@
 			)
 		)
-		(property "Footprint" ""
+		(property "Footprint" "Footprints:0805_RES_RESC2012X60N"
 			(at 49.022 881.38 90)
 			(hide yes)
@@
 			)
 		)
-		(property "Footprint" ""
+		(property "Footprint" "Footprints:0805_RES_RESC2012X60N"
 			(at 49.022 180.34 90)
 			(hide yes)
@@
 			)
 		)
-		(property "Footprint" ""
+		(property "Footprint" "Footprints:0805_RES_RESC2012X60N"
 			(at 49.022 294.64 90)
 			(hide yes)
@@
 			)
 		)
-		(property "Footprint" ""
+		(property "Footprint" "TestPoint:TestPoint_Pad_1.0x1.0mm"
 			(at 139.7 768.35 0)
 			(hide yes)
@@
 			)
 		)
-		(property "Footprint" ""
+		(property "Footprint" "TestPoint:TestPoint_Pad_1.0x1.0mm"
 			(at 139.7 300.99 0)
 			(hide yes)
@@
 			)
 		)
-		(property "Footprint" ""
+		(property "Footprint" "TestPoint:TestPoint_Pad_1.0x1.0mm"
 			(at 139.7 532.13 0)
 			(hide yes)
@@
 			)
 		)
-		(property "Footprint" ""
+		(property "Footprint" "Footprints:0805_RES_RESC2012X60N"
 			(at 49.022 1109.98 90)
 			(hide yes)
@@
 			)
 		)
-		(property "Footprint" ""
+		(property "Footprint" "Footprints:0805_RES_RESC2012X60N"
 			(at 49.022 650.24 90)
 			(hide yes)

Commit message: 10 uF display caps deleted
10 uF display caps ocupy too much space, they were deleted
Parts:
- removed C38, C39, C40, C41, C42, C43, C44, C45, C46, C47, C48: 10uF, Footprints:0805_SMD_TANT_CAP_T491B106K016AT, symbol Device:C

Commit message: big update
coper zones already set, edgecuts set, all components placed, we are just missing the routing
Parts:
- removed C23, C24: 0.1 uF, Footprints:0805_SMD_CERAMIC_CAP_T491B106K016AT, symbol Device:C
- removed DS37, DS38, DS39, DS40, DS41, DS42, DS43, DS44, DS77, DS78, DS79, DS80, DS81, DS82, DS83, DS84, DS85: ACSC03-41EWA-F01, Footprints:SMD_DISPLAY_ACSC03-41EWA-F01, symbol SMD_DISPLAY_ACSC03-41EWA-F01:ACSC03-41EWA-F01
- removed R21, R22: 3v=24.5k, 1.8v=29.8k, Footprints:0805_RES_RESC2012X60N, symbol Device:R
- removed TP10, TP11, TP12, TP13, TP14, TP16, TP17, TP9: TestPoint, TestPoint:TestPoint_Pad_1.0x1.0mm, symbol Connector:TestPoint
- removed U13, U14: MAX7221CWG_, Footprints:Disp_Controler_MAX7221CWG_, symbol Disp_Controler_MAX7221CWG_:MAX7221CWG_
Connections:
- net DIG_4_MAX7221_9: no longer names the net of U12.3 (DIG_4)
- net DIG_5_MAX7221_9: no longer names the net of U12.10 (DIG_5)
- net DIG_6_MAX7221_9: no longer names the net of U12.5 (DIG_6)
- net DIG_7_MAX7221_9: no longer names the net of U12.8 (DIG_7)
- no-connect marks 4 -> 5
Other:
- note removed: "10"
- note removed: "11"
